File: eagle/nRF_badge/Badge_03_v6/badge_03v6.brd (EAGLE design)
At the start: 30 x 70 mm, 43 parts, among them U1 LIS2DH12", U2 LP2985LV, U3 MCP6231, U5 M95M02, Y1 32768Hz

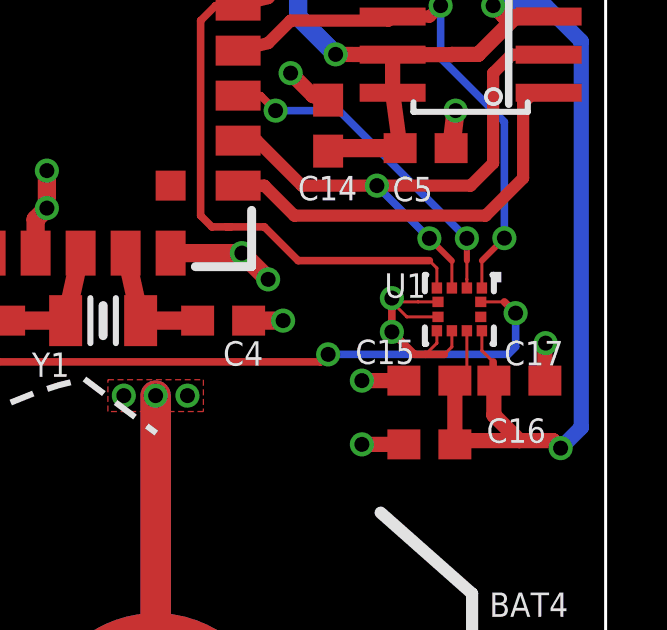
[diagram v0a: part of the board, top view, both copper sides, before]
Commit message: Changes LIS2DH12 footprints to fit the devkit's traces
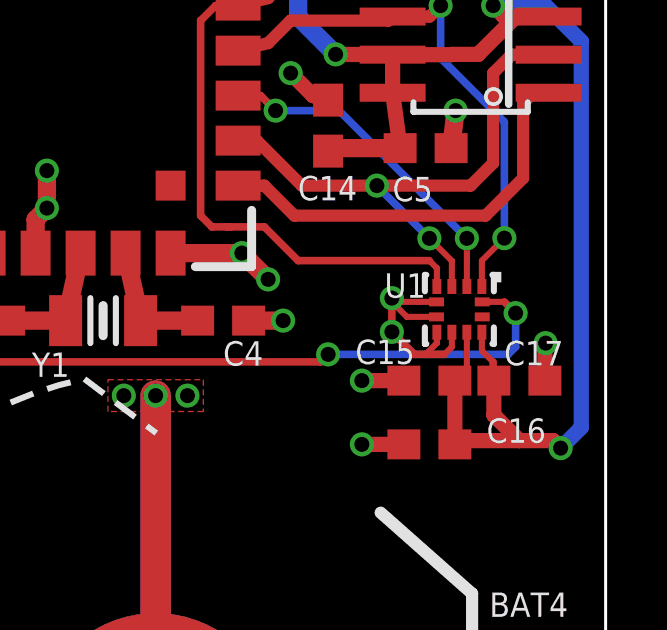
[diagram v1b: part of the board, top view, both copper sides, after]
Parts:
- U1: value LIS2DH12" -> LIS2DH12LIS2DH-DEVKIT; device Badge:LGA12-TN0018-COMPLIANT -> Badge:LGA12-FROM-DEVKIT
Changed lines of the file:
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@@
 <attribute name="VALUE" x="29.53" y="22.99" size="0.8128" layer="27" font="vector" ratio="16" rot="R90"/>
 </element>
-<element name="U1" library="Badge" package="LGA12-TN0018-COMPLIANT" value="LIS2DH12&quot;" x="25.125" y="26.375" smashed="yes" rot="R270">
+<element name="U1" library="Badge" package="LGA12-FROM-DEVKIT" value="LIS2DH12LIS2DH-DEVKIT" x="25.125" y="26.375" smashed="yes" rot="R270">
 <attribute name="NAME" x="24" y="27.575" size="0.8128" layer="25" font="vector" ratio="16" rot="R180"/>
 </element>
@@
 <wire x1="23.275" y1="24" x2="21.875" y2="24" width="0.508" layer="1"/>
 <via x="21.875" y="24" extent="1-16" drill="0.5"/>
-<wire x1="24.875" y1="25.6625" x2="24.875" y2="25.125" width="0.1016" layer="1"/>
-<wire x1="24.875" y1="25.125" x2="24.625" y2="24.875" width="0.1016" layer="1"/>
+<wire x1="24.875" y1="25.6125" x2="24.875" y2="25.125" width="0.2032" layer="1"/>
+<wire x1="24.875" y1="25.125" x2="24.625" y2="24.875" width="0.2032" layer="1"/>
 <wire x1="24" y1="24.875" x2="24.625" y2="24.875" width="0.254" layer="1"/>
 <wire x1="24" y1="24.875" x2="23.625" y2="24.875" width="0.254" layer="1"/>
-<wire x1="24.375" y1="25.6625" x2="24.375" y2="25.25" width="0.1016" layer="1"/>
-<wire x1="24.375" y1="25.25" x2="24" y2="24.875" width="0.1016" layer="1"/>
+<wire x1="24.375" y1="25.6125" x2="24.375" y2="25.25" width="0.2032" layer="1"/>
+<wire x1="24.375" y1="25.25" x2="24" y2="24.875" width="0.2032" layer="1"/>
 <via x="22.875" y="26.75" extent="1-16" drill="0.5"/>
 <wire x1="22.875" y1="25.625" x2="23.625" y2="24.875" width="0.254" layer="1"/>
 <via x="22.875" y="25.625" extent="1-16" drill="0.5"/>
 <wire x1="23" y1="26.625" x2="22.875" y2="26.75" width="0.254" layer="1"/>
-<wire x1="23" y1="26.5" x2="23.375" y2="26.125" width="0.1016" layer="1"/>
+<wire x1="23" y1="26.5" x2="23.375" y2="26.125" width="0.2032" layer="1"/>
 <wire x1="23" y1="26.5" x2="23" y2="26.625" width="0.254" layer="1"/>
 <wire x1="22.875" y1="26.75" x2="22.875" y2="25.625" width="0.254" layer="1"/>
 <wire x1="28" y1="25.25" x2="27.975" y2="25.225" width="0.508" layer="1"/>
 <wire x1="27.975" y1="25.225" x2="27.975" y2="24" width="0.508" layer="1"/>
-<wire x1="23" y1="26.625" x2="23.75" y2="26.625" width="0.1016" layer="1"/>
-<wire x1="23.375" y1="26.125" x2="24.4125" y2="26.125" width="0.1016" layer="1"/>
-<wire x1="23.75" y1="26.625" x2="24.4125" y2="26.625" width="0.1016" layer="1"/>
+<wire x1="23" y1="26.625" x2="23.75" y2="26.625" width="0.2032" layer="1"/>
+<wire x1="23.375" y1="26.125" x2="24.3625" y2="26.125" width="0.2032" layer="1"/>
+<wire x1="23.75" y1="26.625" x2="24.3625" y2="26.625" width="0.2032" layer="1"/>
 </signal>
 <signal name="VCC">
@@
 <contactref element="C16" pad="1"/>
 <wire x1="28.5" y1="21.75" x2="28.25" y2="22" width="0.508" layer="1"/>
-<wire x1="25.875" y1="25.6625" x2="25.875" y2="25" width="0.1016" layer="1"/>
-<wire x1="25.875" y1="25" x2="26.25" y2="24.625" width="0.1016" layer="1"/>
+<wire x1="25.875" y1="25.6125" x2="25.875" y2="25" width="0.2032" layer="1"/>
+<wire x1="25.875" y1="25" x2="26.25" y2="24.625" width="0.2032" layer="1"/>
 <wire x1="26.25" y1="24.625" x2="26.25" y2="24.025" width="0.254" layer="1"/>
 <wire x1="26.25" y1="24.025" x2="26.275" y2="24" width="0.254" layer="1"/>
@@
 <wire x1="24.975" y1="22.125" x2="25.1" y2="22" width="0.508" layer="1"/>
 <wire x1="24.975" y1="24" x2="25.375" y2="24.375" width="0.254" layer="1"/>
-<wire x1="25.375" y1="24.375" x2="25.375" y2="25.6625" width="0.1016" layer="1"/>
+<wire x1="25.375" y1="24.375" x2="25.375" y2="25.6125" width="0.2032" layer="1"/>
 <wire x1="12.175" y1="55.5" x2="14.20394375" y2="55.5" width="0.6096" layer="1"/>
 <wire x1="14.20394375" y1="55.5" x2="14.47394375" y2="55.77" width="0.6096" layer="1"/>
@@
 <via x="26.625" y="28.75" extent="1-16" drill="0.5" diameter="0.8"/>
 <wire x1="26.625" y1="28.75" x2="25.875" y2="28" width="0.2032" layer="1"/>
-<wire x1="25.875" y1="28" x2="25.875" y2="27.0875" width="0.1016" layer="1"/>
+<wire x1="25.875" y1="28" x2="25.875" y2="27.1375" width="0.2032" layer="1"/>
 </signal>
 <signal name="MIC_F">
@@
 <wire x1="17.5" y1="29.125" x2="18.625" y2="29.125" width="0.254" layer="1"/>
 <wire x1="18.625" y1="29.125" x2="19.75" y2="28" width="0.254" layer="1"/>
-<wire x1="24.125" y1="28" x2="24.375" y2="27.75" width="0.1016" layer="1"/>
-<wire x1="24.375" y1="27.75" x2="24.375" y2="27.0875" width="0.1016" layer="1"/>
+<wire x1="24.125" y1="28" x2="24.375" y2="27.75" width="0.2032" layer="1"/>
+<wire x1="24.375" y1="27.75" x2="24.375" y2="27.1375" width="0.2032" layer="1"/>
 <wire x1="19.75" y1="28" x2="24.125" y2="28" width="0.254" layer="1"/>
 </signal>
@@
 <via x="24.125" y="28.742" extent="1-16" drill="0.5" diameter="0.8"/>
 <wire x1="24.125" y1="28.742" x2="24.875" y2="27.992" width="0.2032" layer="1"/>
-<wire x1="24.875" y1="27.992" x2="24.875" y2="27.0875" width="0.1016" layer="1"/>
+<wire x1="24.875" y1="27.992" x2="24.875" y2="27.1375" width="0.2032" layer="1"/>
 <wire x1="24.125" y1="28.742" x2="22.375" y2="30.492" width="0.254" layer="16"/>
 <wire x1="22.375" y1="30.492" x2="22.375" y2="30.5" width="0.254" layer="16"/>
@@
 <contactref element="U1" pad="12"/>
 <contactref element="A1" pad="P$6"/>
-<wire x1="25.8375" y1="26.625" x2="26.625" y2="26.625" width="0.1016" layer="1"/>
+<wire x1="25.8875" y1="26.625" x2="26.625" y2="26.625" width="0.2032" layer="1"/>
 <wire x1="26.625" y1="26.625" x2="27" y2="26.25" width="0.254" layer="1"/>
 <via x="27" y="26.25" extent="1-16" drill="0.5" diameter="0.8"/>
@@
 <via x="25.375" y="28.742" extent="1-16" drill="0.5" diameter="0.8"/>
 <wire x1="25.375" y1="28.742" x2="25.375" y2="28" width="0.2032" layer="1"/>
-<wire x1="25.375" y1="28" x2="25.375" y2="27.375" width="0.1016" layer="1"/>
-<wire x1="25.375" y1="27.375" x2="25.375" y2="27.0875" width="0.1016" layer="1"/>
+<wire x1="25.375" y1="28" x2="25.375" y2="27.375" width="0.2032" layer="1"/>
+<wire x1="25.375" y1="27.375" x2="25.375" y2="27.1375" width="0.1016" layer="1"/>
 </signal>
 </signals>
